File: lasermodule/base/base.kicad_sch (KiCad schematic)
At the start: 18 parts, among them J10 Conn_01x01, J11 Conn_01x01, J12 Conn_01x01, J19 2-84952-0, J2 Conn_01x13, J6 mirrormotor, J7 Conn_01x01, J8 Conn_01x01, J9 Conn_01x01

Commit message: fixes some mistake in the bom found in first assembly
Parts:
- H1, H2, H3, H4: now in the parts list
- L1, L2, L3, L4, L5: now left out of the parts list
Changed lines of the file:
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@@
 		(unit 1)
 		(exclude_from_sim no)
-		(in_bom yes)
+		(in_bom no)
 		(on_board yes)
 		(dnp no)
@@
 		(unit 1)
 		(exclude_from_sim yes)
-		(in_bom no)
+		(in_bom yes)
 		(on_board yes)
 		(dnp no)
@@
 		(unit 1)
 		(exclude_from_sim no)
-		(in_bom yes)
+		(in_bom no)
 		(on_board yes)
 		(dnp no)
@@
 		(unit 1)
 		(exclude_from_sim yes)
-		(in_bom no)
+		(in_bom yes)
 		(on_board yes)
 		(dnp no)
@@
 		(unit 1)
 		(exclude_from_sim yes)
-		(in_bom no)
+		(in_bom yes)
 		(on_board yes)
 		(dnp no)
@@
 		(unit 1)
 		(exclude_from_sim no)
-		(in_bom yes)
+		(in_bom no)
 		(on_board yes)
 		(dnp no)
@@
 		(unit 1)
 		(exclude_from_sim no)
-		(in_bom yes)
+		(in_bom no)
 		(on_board yes)
 		(dnp no)
@@
 		(unit 1)
 		(exclude_from_sim yes)
-		(in_bom no)
+		(in_bom yes)
 		(on_board yes)
 		(dnp no)
@@
 		(unit 1)
 		(exclude_from_sim no)
-		(in_bom yes)
-		(on_board yes)
-		(dnp no)
+		(in_bom no)
+		(on_board yes)
+		(dnp no)

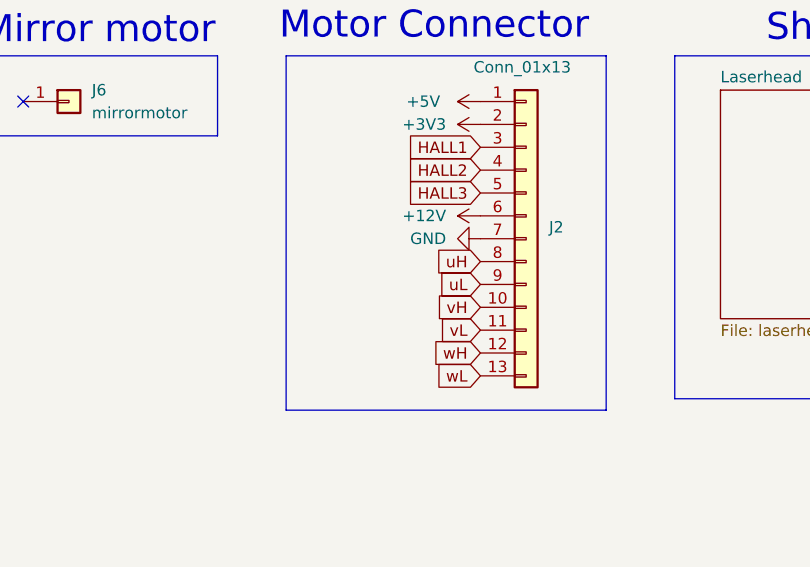
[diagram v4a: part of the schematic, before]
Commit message: fixed headers, shifted text base board
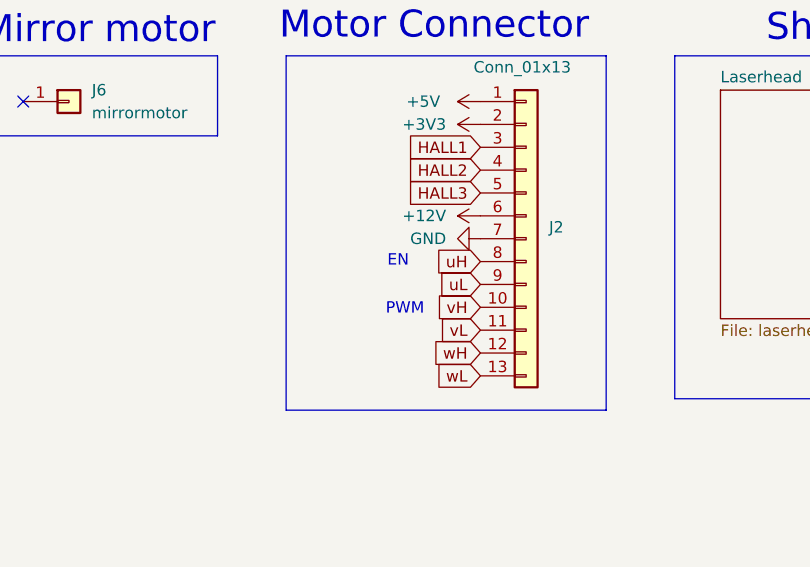
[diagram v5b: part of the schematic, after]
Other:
- note added: "EN"
- note added: "PWM"
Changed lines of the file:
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@@
+		)
+	)
+	(text "PWM"
+		(exclude_from_sim no)
+		(at 171.958 70.104 0)
+		(effects
+			(font
+				(size 1.27 1.27)
+			)
 		)
 	)
@@
 		)
 	)
+	(text "EN"
+		(exclude_from_sim no)
+		(at 171.196 64.77 0)
+		(effects
+			(font
+				(size 1.27 1.27)
+			)
+		)
+	)
